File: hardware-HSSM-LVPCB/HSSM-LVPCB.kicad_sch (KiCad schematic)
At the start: 61 parts, among them J1 UFL_R_SMT_1_10, Q1 Q_MOSFET_N_BSS123, Q2 Q_MOSFET_N_BSS123, U1 ESP32-C6, U2 W25Q64JVSSIQ_SOIC-8, U3 U_USB_UART_CP2102-GMR, U4 U_EnvSensor_BME280_LGA_Bosch, U5 U_AirQualitySensor_ENS160_BGLM, X1 X_40MHz_SMD_ECS-2520SMV-400-F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

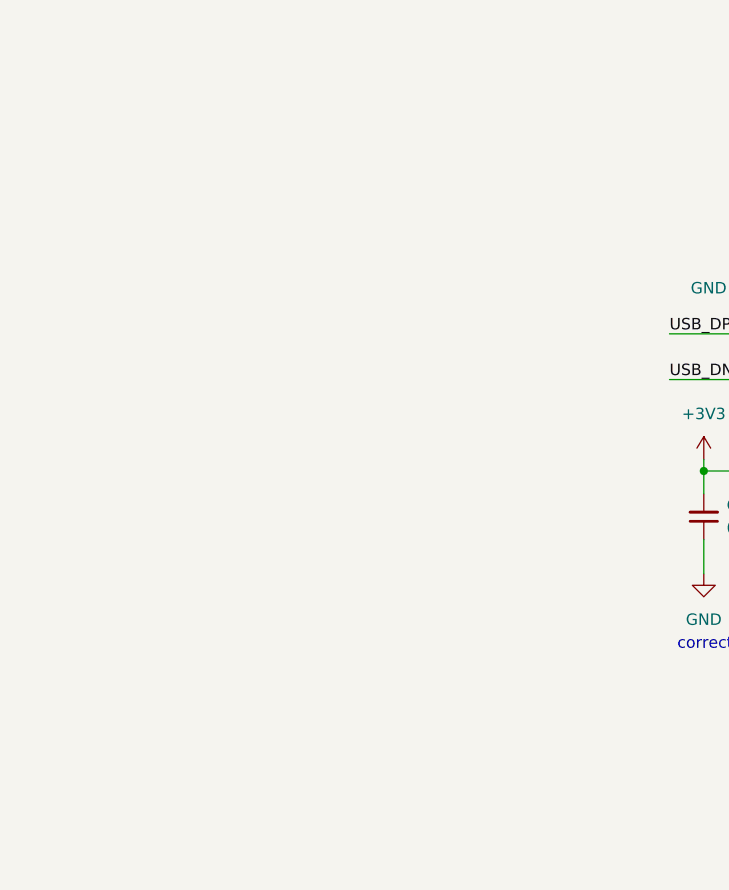
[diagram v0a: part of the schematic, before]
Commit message: [#4] Add TSM-106-01-L-SH
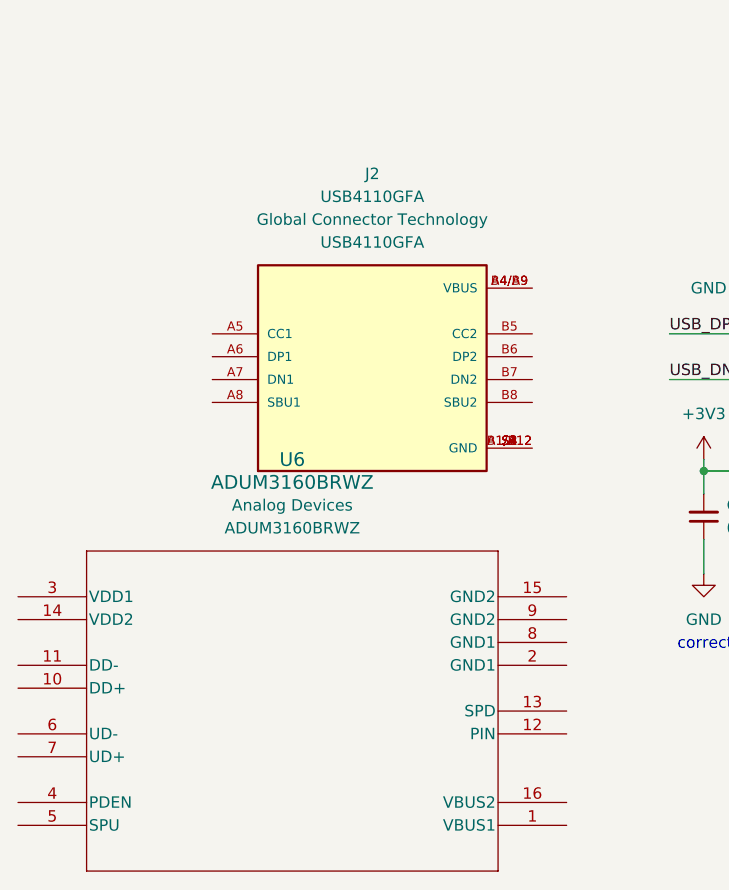
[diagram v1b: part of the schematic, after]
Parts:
- added J2: USB4110GFA, HSSM-LVPCB:GCT_USB4110GFA, symbol HSSM-LVPCB:USB4110GFA
- added U6: ADUM3160BRWZ, HSSM-LVPCB:ADUM3160BRWZ, symbol HSSM-LVPCB:ADUM3160BRWZ
- CON1: footprint (none) -> HSSM-LVPCB:FFC_solder_connector_16pos
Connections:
- new net: J2.A1/B12 (GND), J2.B1/A12 (GND), J2.S1 (GND), J2.S2 (GND), J2.S3 (GND), J2.S4 (GND)
- new net: J2.A4/B9 (VBUS), J2.B4/A9 (VBUS)

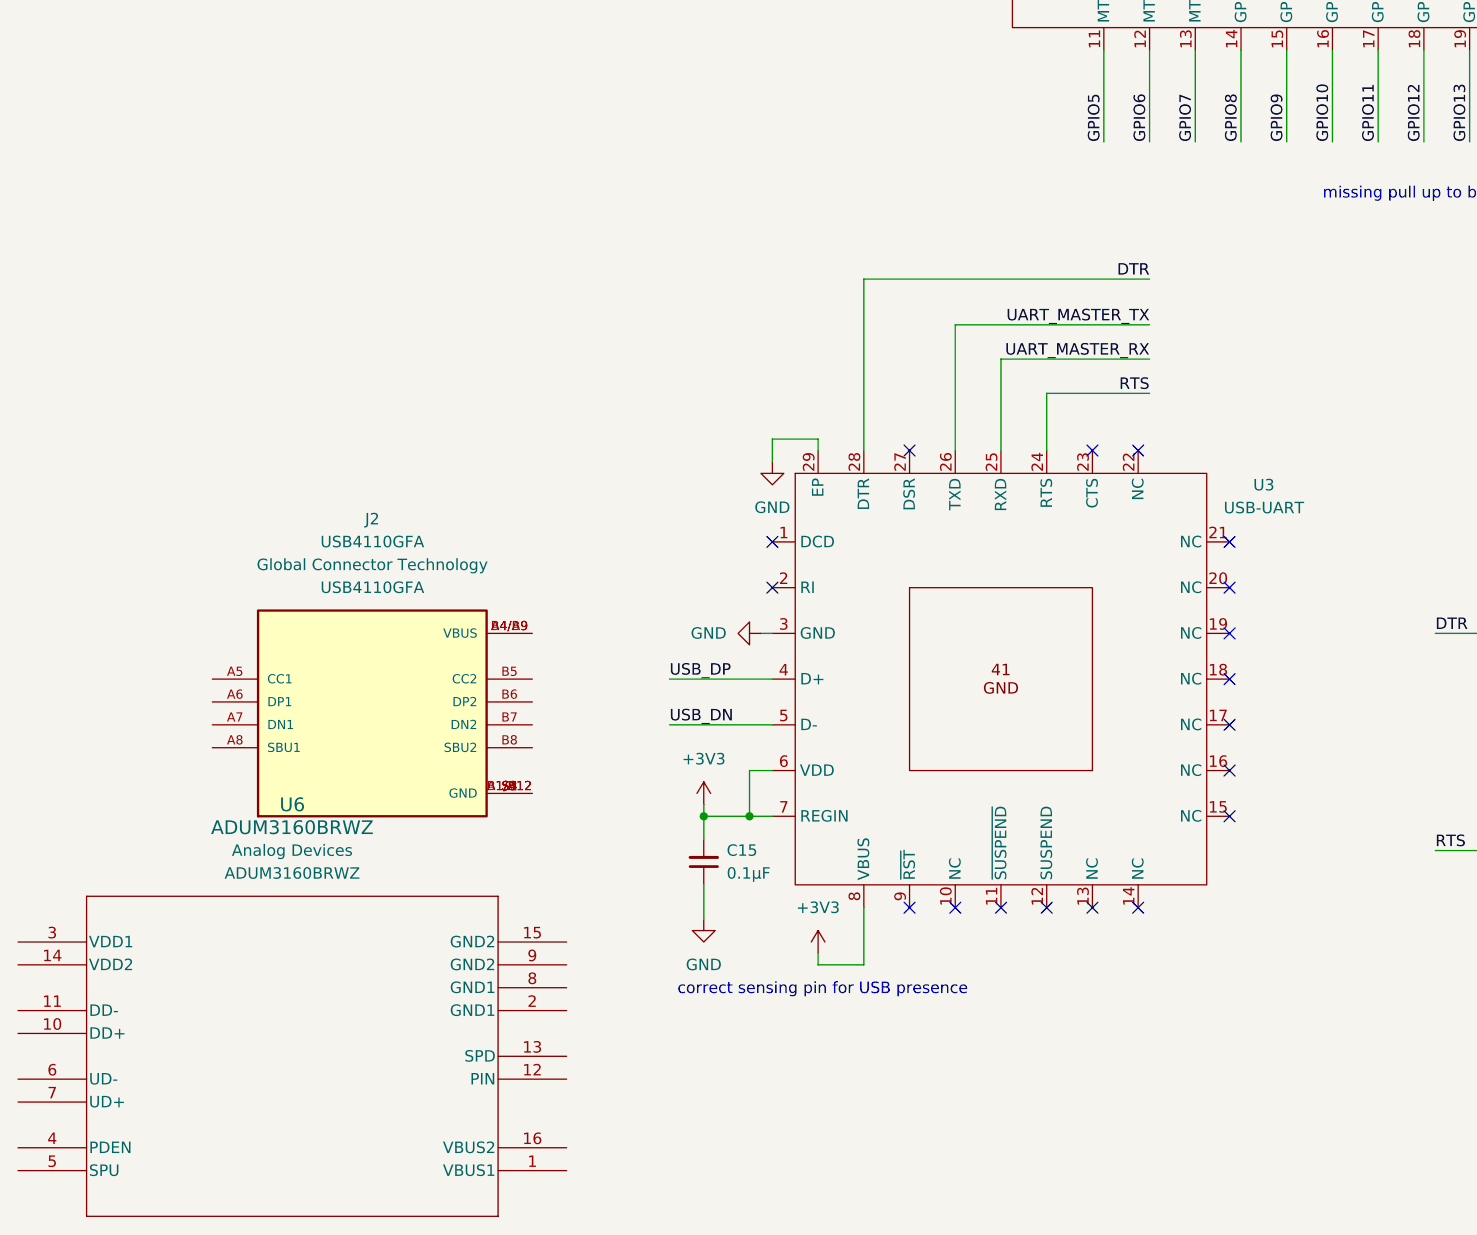
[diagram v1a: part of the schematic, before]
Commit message: [#9] Add programming connector
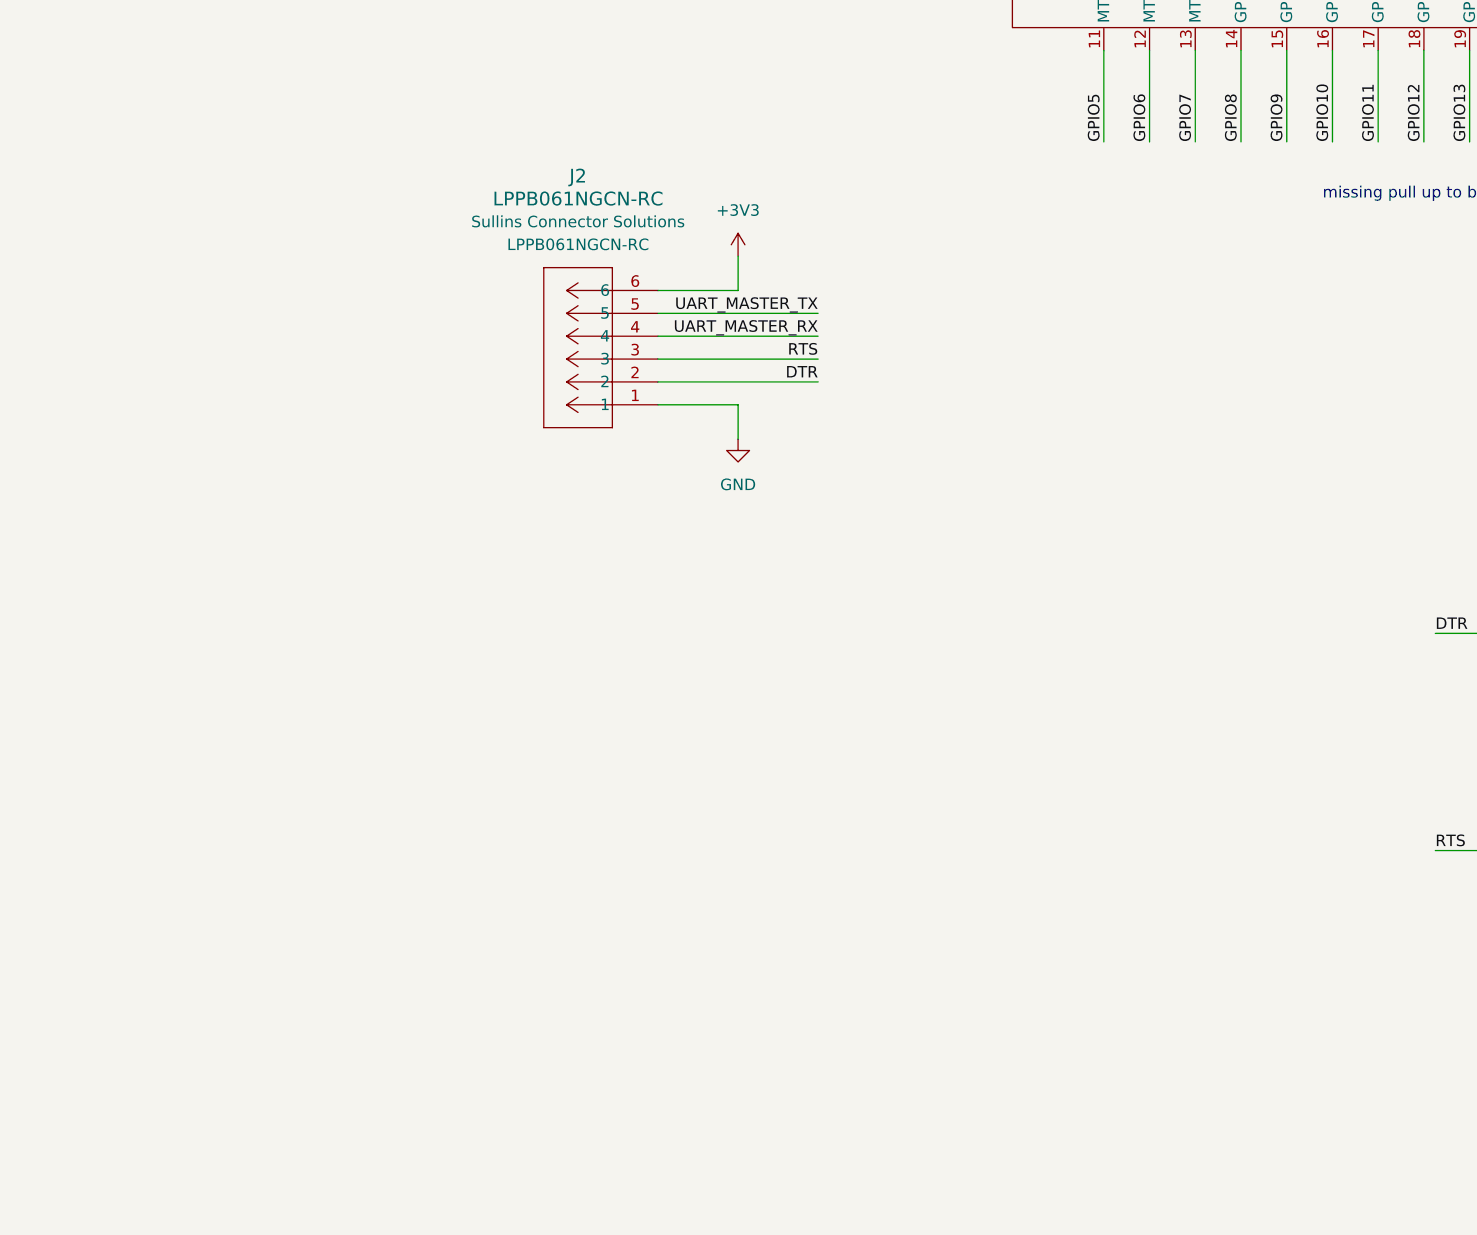
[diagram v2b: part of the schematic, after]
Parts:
- removed C15: C_0u1_10pct_50V_0402_GRM155R71H104KE14D, HSSM-LVPCB:C_0402, symbol HSSM-LVPCB:C_0u1_10pct_50V_0402_GRM155R71H104KE14D
- removed J2: USB4110GFA, HSSM-LVPCB:GCT_USB4110GFA, symbol HSSM-LVPCB:USB4110GFA
- removed U3: U_USB_UART_CP2102-GMR, HSSM-LVPCB:QFN-28-1EP_4x4mm_P0.4mm_EP2.3x2.3mm, symbol HSSM-LVPCB:U_USB_UART_CP2102-GMR
- removed U6: ADUM3160BRWZ, HSSM-LVPCB:ADUM3160BRWZ, symbol HSSM-LVPCB:ADUM3160BRWZ
- added J2: LPPB061NGCN-RC, HSSM-LVPCB:LPPB061NGCN-RC, symbol HSSM-LVPCB:FemalePinHeader_1x06_1.27mm_LPPB061NGCN-RC
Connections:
- net +3V3: now also J2.6
- net DTR: now also J2.2
- net GND: now also J2.1
- net RTS: now also J2.3
- net UART_MASTER_RX: now also J2.4
- net UART_MASTER_TX: now also J2.5
- no-connect marks 18 -> 0
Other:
- note removed: "correct sensing pin for USB presence"

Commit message: [#2] Mockup of the device
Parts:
- added R20, R21: R_10k_1pct_0402_RC0402FR-0710KL, HSSM-LVPCB:R_0402, symbol HSSM-LVPCB:R_10k_1pct_0402_RC0402FR-0710KL
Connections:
- net +3V3: now also R20.2, R21.2
- net DTR: now also R20.1
- net RTS: now also R21.1

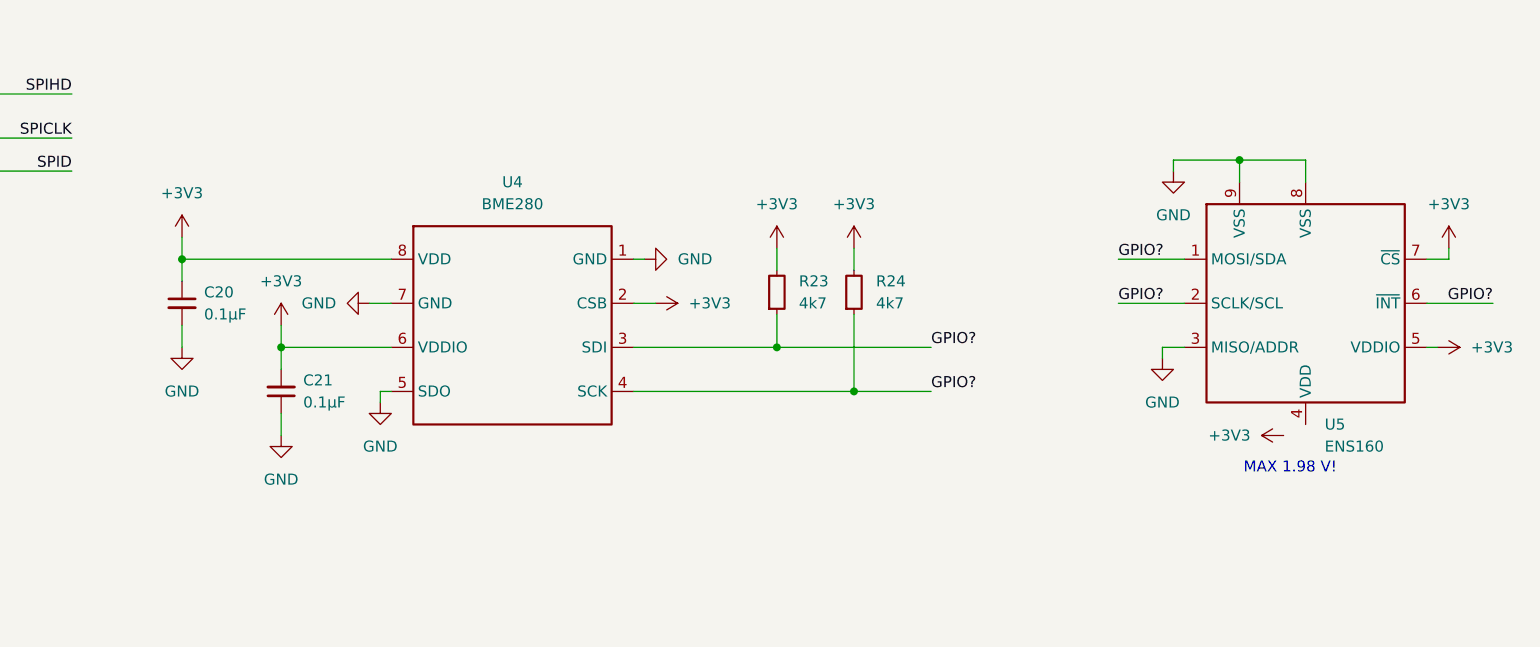
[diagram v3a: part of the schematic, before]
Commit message: [#4] SCH removed additional sensors
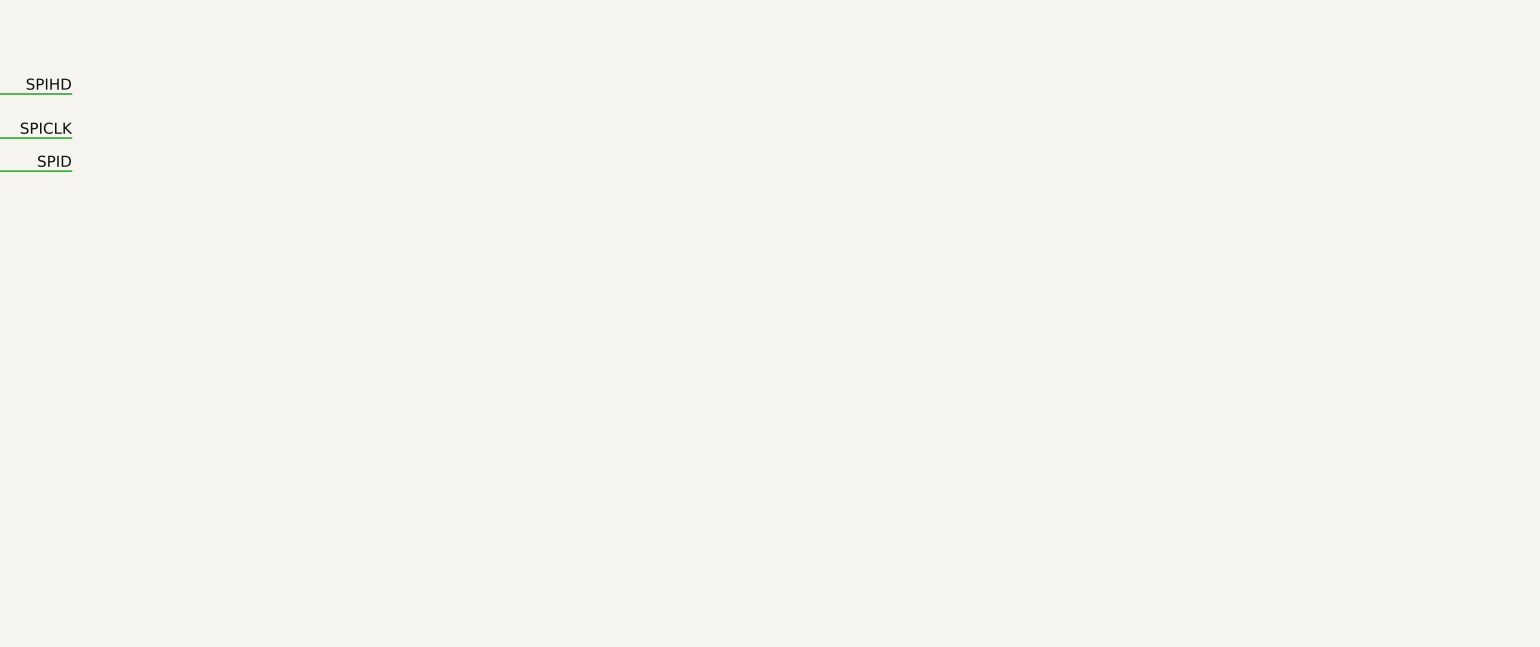
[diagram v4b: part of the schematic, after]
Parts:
- removed C20, C21: C_0u1_10pct_50V_0402_GRM155R71H104KE14D, HSSM-LVPCB:C_0402, symbol HSSM-LVPCB:C_0u1_10pct_50V_0402_GRM155R71H104KE14D
- removed R23, R24: R_4k7_0402, HSSM-LVPCB:R_0402, symbol HSSM-LVPCB:R_4k7_0402
- removed U4: U_EnvSensor_BME280_LGA_Bosch, HSSM-LVPCB:Bosch_LGA-8_2.5x2.5mm_P0.65mm_ClockwisePinNumbering, symbol HSSM-LVPCB:U_EnvSensor_BME280_LGA_Bosch
- removed U5: U_AirQualitySensor_ENS160_BGLM, HSSM-LVPCB:XDCR_ENS160-BGLM, symbol HSSM-LVPCB:U_AirQualitySensor_ENS160_BGLM
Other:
- note removed: "MAX 1.98 V!"
